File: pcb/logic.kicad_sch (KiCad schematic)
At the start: 62 parts, among them Q100 2N7002, Q101 2N7002, Q102 2N7002, Q103 2N7002, Q104 2N7002, Q105 2N7002, Q106 2N7002, Q107 2N7002, Q108 2N7002, Q109 2N7002, Q110 2N7002, Q111 2N7002, Q112 2N7002, Q113 2N7002, Q114 2N7002, Q115 2N7002, Q116 2N7002, Q117 2N7002, Q118 2N7002, Q119 2N7002, Q120 2N7002, Q121 2N7002, Q122 2N7002, Q123 2N7002, Q124 2N7002, Q125 2N7002, Q126 2N7002, Q127 2N7002, Q128 2N7002, Q129 2N7002, Q130 2N7002, Q131 2N7002, Q132 2N7002, Q133 2N7002, Q134 2N7002, Q135 2N7002, Q136 2N7002, Q137 2N7002, Q138 2N7002, Q139 2N7002, Q140 2N7002, Q97 2N7002, Q98 2N7002, Q99 2N7002

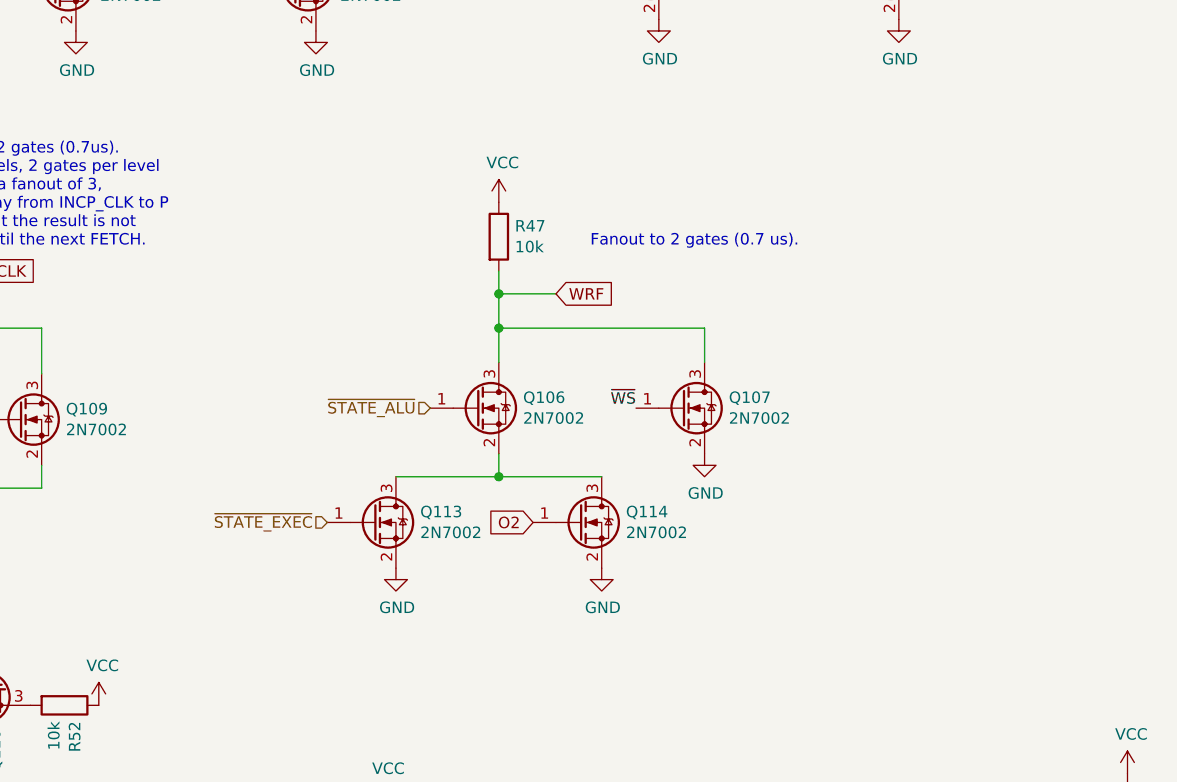
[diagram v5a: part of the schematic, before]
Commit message: Fix flag for lea.
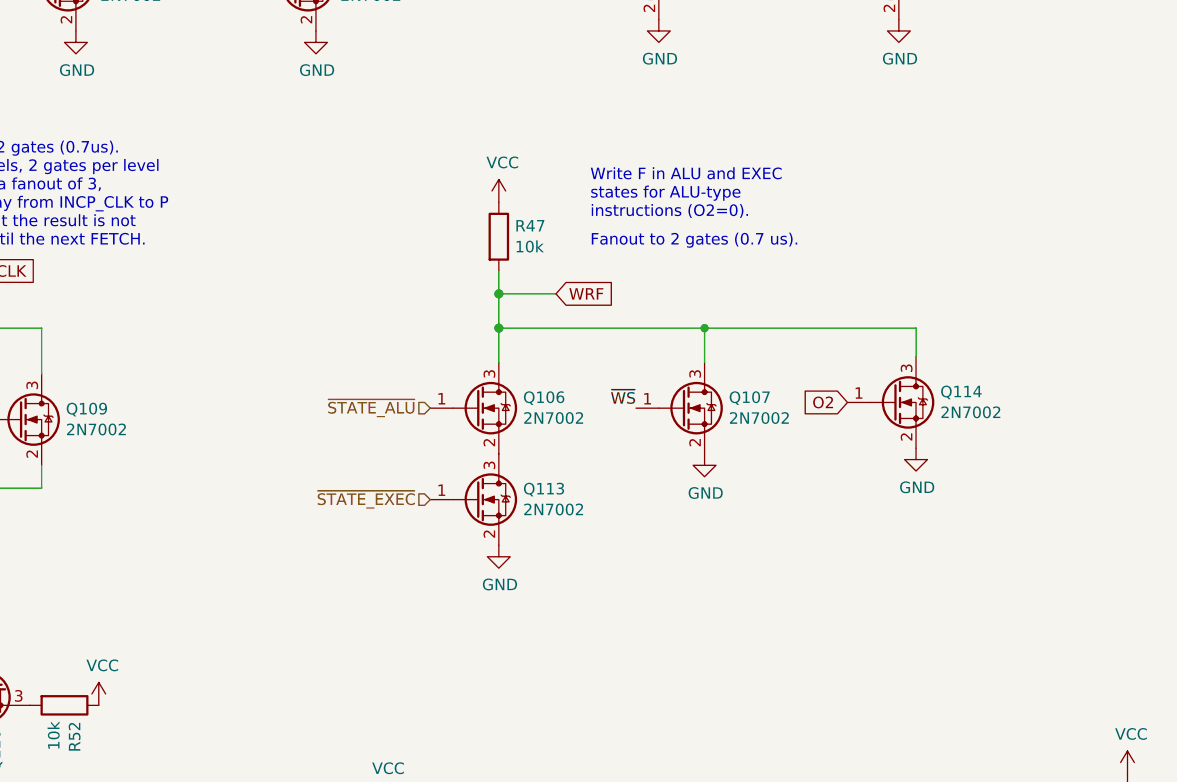
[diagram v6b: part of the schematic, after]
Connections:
- net WRF: now also Q114.3 (D)
- net at Q106.2 (S), Q113.3 (D): no longer Q114.3 (D)
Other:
- note added: "Write F in ALU and EXEC states for ALU-type instructions (O2=0)."
- moved on the sheet: Q113, Q114
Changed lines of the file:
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@@
   (junction (at 209.55 83.82) (diameter 1.016) (color 0 0 0 0))
   (junction (at 209.55 87.63) (diameter 1.016) (color 0 0 0 0))
-  (junction (at 209.55 104.14) (diameter 1.016) (color 0 0 0 0))
   (junction (at 227.33 38.1) (diameter 1.016) (color 0 0 0 0))
   (junction (at 227.33 172.72) (diameter 1.016) (color 0 0 0 0))
+  (junction (at 232.41 87.63) (diameter 0.9144) (color 0 0 0 0))
   (junction (at 246.38 38.1) (diameter 1.016) (color 0 0 0 0))
   (junction (at 279.4 151.13) (diameter 1.016) (color 0 0 0 0))
@@
     (stroke (width 0) (type solid) (color 0 0 0 0))
   )
-  (wire (pts (xy 198.12 104.14) (xy 209.55 104.14))
-    (stroke (width 0) (type solid) (color 0 0 0 0))
-  )
   (wire (pts (xy 204.47 147.32) (xy 204.47 153.67))
     (stroke (width 0) (type solid) (color 0 0 0 0))
@@
     (stroke (width 0) (type solid) (color 0 0 0 0))
   )
-  (wire (pts (xy 209.55 104.14) (xy 209.55 101.6))
-    (stroke (width 0) (type solid) (color 0 0 0 0))
-  )
-  (wire (pts (xy 209.55 104.14) (xy 220.98 104.14))
-    (stroke (width 0) (type solid) (color 0 0 0 0))
-  )
   (wire (pts (xy 209.55 147.32) (xy 204.47 147.32))
     (stroke (width 0) (type solid) (color 0 0 0 0))
@@
   )
   (wire (pts (xy 254 38.1) (xy 254 43.18))
+    (stroke (width 0) (type solid) (color 0 0 0 0))
+  )
+  (wire (pts (xy 255.905 87.63) (xy 232.41 87.63))
+    (stroke (width 0) (type solid) (color 0 0 0 0))
+  )
+  (wire (pts (xy 255.905 90.805) (xy 255.905 87.63))
     (stroke (width 0) (type solid) (color 0 0 0 0))
   )
@@
     (effects (font (size 1.27 1.27)) (justify left bottom))
   )
+  (text "Write F in ALU and EXEC\nstates for ALU-type\ninstructions (O2=0)."
+    (at 219.71 75.565 0)
+    (effects (font (size 1.27 1.27)) (justify left bottom))
+  )
   (text "Fanout to 2 gates (0.7 us)." (at 219.71 78.74 0)
     (effects (font (size 1.27 1.27)) (justify left bottom))
@@
     )
   )
-  (global_label "O2" (shape input) (at 213.36 109.22 180)
-    (effects (font (size 1.27 1.27)) (justify right))
-    (property "Intersheet References" "${INTERSHEET_REFS}" (id 0) (at 55.88 -53.34 0)
-      (effects (font (size 1.27 1.27)) hide)
-    )
-  )
   (global_label "WRF" (shape input) (at 215.9 83.82 0)
     (effects (font (size 1.27 1.27)) (justify left))
@@
     )
   )
+  (global_label "O2" (shape input) (at 248.285 95.885 180)
+    (effects (font (size 1.27 1.27)) (justify right))
+    (property "Intersheet References" "${INTERSHEET_REFS}" (id 0) (at 90.805 -66.675 0)
+      (effects (font (size 1.27 1.27)) hide)
+    )
+  )
   (global_label "XHIN_DBUS" (shape input) (at 294.64 35.56 0)
     (effects (font (size 1.27 1.27)) (justify left))
@@
     (effects (font (size 1.27 1.27)) (justify right))
   )
-  (hierarchical_label "~STATE_EXEC" (shape input) (at 190.5 109.22 180)
-    (effects (font (size 1.27 1.27)) (justify right))
-  )
   (hierarchical_label "~STATE_ALU" (shape input) (at 201.93 96.52 180)
+    (effects (font (size 1.27 1.27)) (justify right))
+  )
+  (hierarchical_label "~STATE_EXEC" (shape input) (at 201.93 106.68 180)
     (effects (font (size 1.27 1.27)) (justify right))
   )
@@
     (pin "1")
   )
-  (symbol (lib_id "power:GND") (at 198.12 114.3 0) (unit 1)
-    (in_bom yes) (on_board yes)
-    (property "Reference" "#PWR0121" (id 0) (at 198.12 120.65 0)
-      (effects (font (size 1.27 1.27)) hide)
-    )
-    (property "Value" "GND" (id 1) (at 198.247 118.6942 0))
-    (property "Footprint" "" (id 2) (at 198.12 114.3 0)
-      (effects (font (size 1.27 1.27)) hide)
-    )
-    (property "Datasheet" "" (id 3) (at 198.12 114.3 0)
-      (effects (font (size 1.27 1.27)) hide)
-    )
-    (pin "1")
-  )
   (symbol (lib_id "power:GND") (at 208.28 204.47 0) (unit 1)
     (in_bom yes) (on_board yes)
@@
     (pin "1")
   )
-  (symbol (lib_id "power:GND") (at 220.98 114.3 0) (unit 1)
-    (in_bom yes) (on_board yes)
-    (property "Reference" "#PWR0122" (id 0) (at 220.98 120.65 0)
-      (effects (font (size 1.27 1.27)) hide)
-    )
-    (property "Value" "GND" (id 1) (at 221.107 118.6942 0))
-    (property "Footprint" "" (id 2) (at 220.98 114.3 0)
-      (effects (font (size 1.27 1.27)) hide)
-    )
-    (property "Datasheet" "" (id 3) (at 220.98 114.3 0)
+  (symbol (lib_id "power:GND") (at 209.55 111.76 0) (unit 1)
+    (in_bom yes) (on_board yes)
+    (property "Reference" "#PWR0121" (id 0) (at 209.55 118.11 0)
+      (effects (font (size 1.27 1.27)) hide)
+    )
+    (property "Value" "GND" (id 1) (at 209.677 116.1542 0))
+    (property "Footprint" "" (id 2) (at 209.55 111.76 0)
+      (effects (font (size 1.27 1.27)) hide)
+    )
+    (property "Datasheet" "" (id 3) (at 209.55 111.76 0)
       (effects (font (size 1.27 1.27)) hide)
     )
@@
     )
     (property "Datasheet" "" (id 3) (at 254 53.34 0)
+      (effects (font (size 1.27 1.27)) hide)
+    )
+    (pin "1")
+  )
+  (symbol (lib_id "power:GND") (at 255.905 100.965 0) (unit 1)
+    (in_bom yes) (on_board yes)
+    (property "Reference" "#PWR0122" (id 0) (at 255.905 107.315 0)
+      (effects (font (size 1.27 1.27)) hide)
+    )
+    (property "Value" "GND" (id 1) (at 256.032 105.3592 0))
+    (property "Footprint" "" (id 2) (at 255.905 100.965 0)
+      (effects (font (size 1.27 1.27)) hide)
+    )
+    (property "Datasheet" "" (id 3) (at 255.905 100.965 0)
       (effects (font (size 1.27 1.27)) hide)
     )
@@
     (pin "3")
   )
-  (symbol (lib_id "Transistor_FET:2N7002") (at 195.58 109.22 0) (unit 1)
-    (in_bom yes) (on_board yes)
-    (property "Reference" "Q113" (id 0) (at 200.8124 108.0516 0)
-      (effects (font (size 1.27 1.27)) (justify left))
-    )
-    (property "Value" "2N7002" (id 1) (at 200.8124 110.363 0)
-      (effects (font (size 1.27 1.27)) (justify left))
-    )
-    (property "Footprint" "Package_TO_SOT_SMD:SOT-23" (id 2) (at 200.66 111.125 0)
-      (effects (font (size 1.27 1.27) italic) (justify left) hide)
-    )
-    (property "Datasheet" "https://datasheet.lcsc.com/szlcsc/Guangdong-Hottech-2N7002K_C181083.pdf" (id 3) (at 195.58 109.22 0)
-      (effects (font (size 1.27 1.27)) (justify left) hide)
-    )
-    (property "LCSC" "C181083" (id 4) (at 195.58 109.22 0)
-      (effects (font (size 1.27 1.27)) hide)
-    )
-    (pin "1")
-    (pin "2")
-    (pin "3")
-  )
   (symbol (lib_id "Transistor_FET:2N7002") (at 205.74 199.39 0) (unit 1)
     (in_bom yes) (on_board yes)
@@
     (pin "3")
   )
-  (symbol (lib_id "Transistor_FET:2N7002") (at 218.44 109.22 0) (unit 1)
-    (in_bom yes) (on_board yes)
-    (property "Reference" "Q114" (id 0) (at 223.6724 108.0516 0)
-      (effects (font (size 1.27 1.27)) (justify left))
-    )
-    (property "Value" "2N7002" (id 1) (at 223.6724 110.363 0)
-      (effects (font (size 1.27 1.27)) (justify left))
-    )
-    (property "Footprint" "Package_TO_SOT_SMD:SOT-23" (id 2) (at 223.52 111.125 0)
-      (effects (font (size 1.27 1.27) italic) (justify left) hide)
-    )
-    (property "Datasheet" "https://datasheet.lcsc.com/szlcsc/Guangdong-Hottech-2N7002K_C181083.pdf" (id 3) (at 218.44 109.22 0)
-      (effects (font (size 1.27 1.27)) (justify left) hide)
-    )
-    (property "LCSC" "C181083" (id 4) (at 218.44 109.22 0)
+  (symbol (lib_id "Transistor_FET:2N7002") (at 207.01 106.68 0) (unit 1)
+    (in_bom yes) (on_board yes)
+    (property "Reference" "Q113" (id 0) (at 212.2424 105.5116 0)
+      (effects (font (size 1.27 1.27)) (justify left))
+    )
+    (property "Value" "2N7002" (id 1) (at 212.2424 107.823 0)
+      (effects (font (size 1.27 1.27)) (justify left))
+    )
+    (property "Footprint" "Package_TO_SOT_SMD:SOT-23" (id 2) (at 212.09 108.585 0)
+      (effects (font (size 1.27 1.27) italic) (justify left) hide)
+    )
+    (property "Datasheet" "https://datasheet.lcsc.com/szlcsc/Guangdong-Hottech-2N7002K_C181083.pdf" (id 3) (at 207.01 106.68 0)
+      (effects (font (size 1.27 1.27)) (justify left) hide)
+    )
+    (property "LCSC" "C181083" (id 4) (at 207.01 106.68 0)
       (effects (font (size 1.27 1.27)) hide)
     )
@@
       (effects (font (size 1.27 1.27)) hide)
     )
+    (pin "1")
+    (pin "2")
+    (pin "3")
+  )
+  (symbol (lib_id "Transistor_FET:2N7002") (at 253.365 95.885 0) (unit 1)
+    (in_bom yes) (on_board yes)
+    (property "Reference" "Q114" (id 0) (at 258.5974 94.7166 0)
+      (effects (font (size 1.27 1.27)) (justify left))
+    )
+    (property "Value" "2N7002" (id 1) (at 258.5974 97.028 0)
+      (effects (font (size 1.27 1.27)) (justify left))
+    )
+    (property "Footprint" "Package_TO_SOT_SMD:SOT-23" (id 2) (at 258.445 97.79 0)
+      (effects (font (size 1.27 1.27) italic) (justify left) hide)
+    )
+    (property "Datasheet" "https://datasheet.lcsc.com/szlcsc/Guangdong-Hottech-2N7002K_C181083.pdf" (id 3) (at 253.365 95.885 0)
+      (effects (font (size 1.27 1.27)) (justify left) hide)
+    )
+    (property "LCSC" "C181083" (id 4) (at 253.365 95.885 0)
+      (effects (font (size 1.27 1.27)) hide)
+    )

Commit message: Revision 3.
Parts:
- added Q1093, Q1094: 2N7002, Package_TO_SOT_SMD:SOT-23, symbol Transistor_FET:2N7002
- Q115, Q117, Q132: value 2N7002 -> 2N7002K
- R52: value 10k -> 1k; LCSC C17414 -> C17513
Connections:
- net GND: now also Q1093.2 (S); no longer Q97.2 (S)
- net VCC: now also R52.2; no longer R52.1
- net at Q121.2 (S): now also Q1094.3 (D); no longer Q127.3 (D)
- net at Q116.3 (D): now also R52.1; no longer R52.2
- new net: Q1094.2 (S), Q127.3 (D)
- new net: Q1093.3 (D), Q97.2 (S)
- new net ~STATE_DEREF: Q1093.1 (G), Q1094.1 (G)
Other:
- moved on the sheet: Q127, Q98, R46

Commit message: Snake.
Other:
- note added: "Relative (Z=0) Fanout to 6 gates (2us)"
- note removed: "Relative (Z=0) Fanout to 5 gates (1.7us)"
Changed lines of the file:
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@@
     (effects (font (size 1.27 1.27)) (justify left bottom))
   )
-  (text "Relative (Z=0)\nFanout to 5 gates (1.7us)" (at 170.18 30.48 0)
+  (text "Relative (Z=0)\nFanout to 6 gates (2us)" (at 170.18 30.48 0)
     (effects (font (size 1.27 1.27)) (justify left bottom))
   )
